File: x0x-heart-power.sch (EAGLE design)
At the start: 13 parts, among them IC1 7805T, IC2 7812T, X0X-HEART POWER

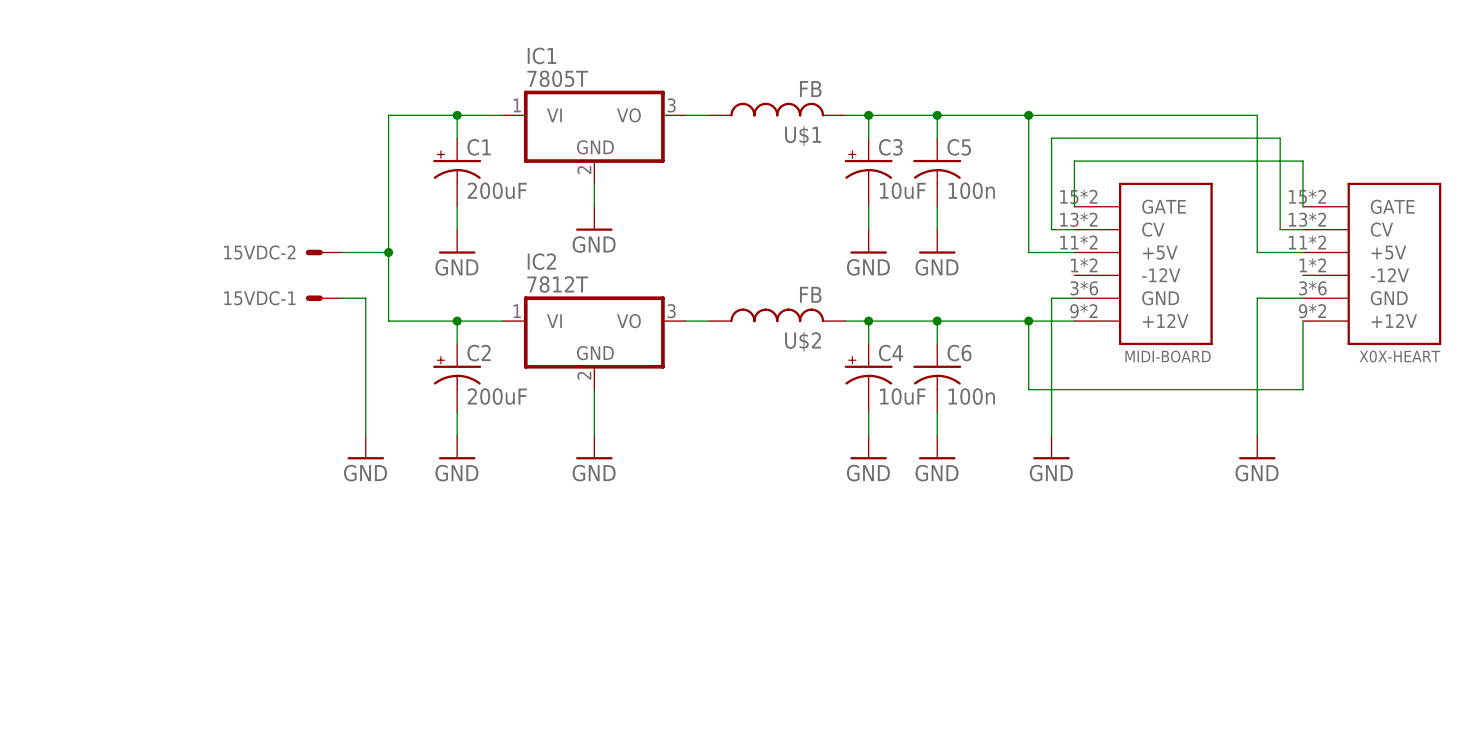
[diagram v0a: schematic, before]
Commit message: added negative 12
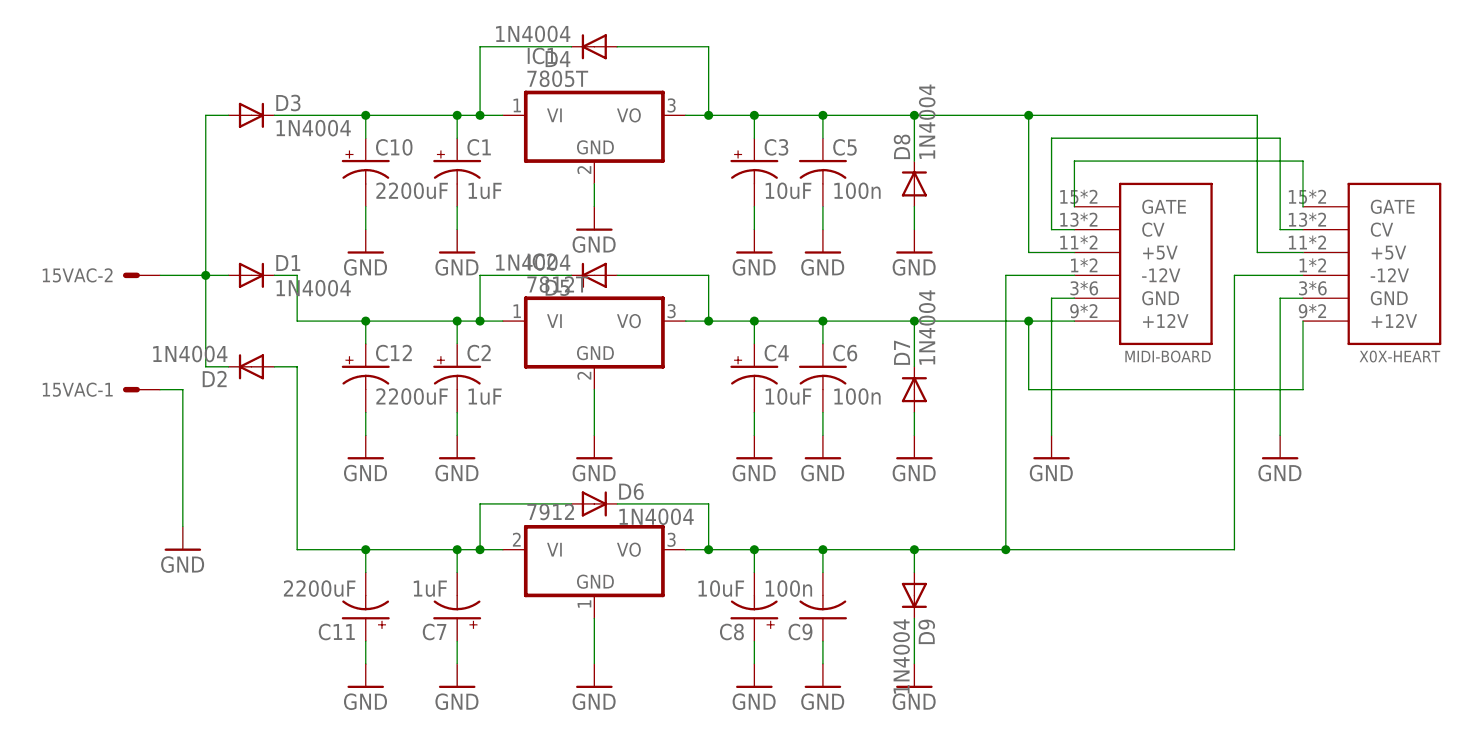
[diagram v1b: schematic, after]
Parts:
- removed 15VDC: (no value), con-molex:KK-156-2
- removed U$1, U$2: FB, adafruit:FB
- added 15VAC: (no value), con-molex:KK-156-2
- added 7912: (no value), linear:7912T
- added C10, C11, C12: 2200uF, rcl:CPOL-USE22-6AXIAL
- added C7: 1uF, rcl:CPOL-USE2-5
- added C8: 10uF, rcl:CPOL-USE2-5
- added C9: 100n, rcl:C-US025-024X044
- added D1, D2, D3, D4, D5, D6, D7, D8, D9: 1N4004, diode:1N4004
- C1, C2: value 200uF -> 1uF; device rcl:CPOL-USE22-6AXIAL -> rcl:CPOL-USE2-5
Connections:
- new net N$8: C12.+, C2.+, D1.C, D5.C, IC2.VI
- new net N$9: 15VAC-2.S, D1.A, D2.C, D3.A
- net GND: now also 15VAC-1.S, 7912.GND, C10.-, C11.+, C12.-, C7.+, C8.+, C9.1, D7.A, D8.A, D9.C; no longer 15VDC-1.S
- net N$3: now also D4.A, D8.C, IC1.VO; no longer U$1.2
- net N$4: now also 7912.VI, C11.-, C7.-, D2.A, D6.A; no longer IC1.VO, U$1.1
- net N$5: now also 7912.VO, C8.-, C9.2, D6.C, D9.A, MIDI-BOARD.-12V, X0X-HEART.-12V; no longer C4.+, C6.1, MIDI-BOARD.+12V, U$2.2, X0X-HEART.+12V
- net N$6: now also C10.+, D3.C, D4.C; no longer 15VDC-2.S, C2.+, IC2.VI
- net N$7: now also C4.+, C6.1, D5.A, D7.C, MIDI-BOARD.+12V, X0X-HEART.+12V; no longer U$2.1
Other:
- moved on the sheet: C3, C4, C5, C6
